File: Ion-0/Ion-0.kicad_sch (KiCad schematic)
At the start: 11 parts, among them J3 Conn_02x06_Odd_Even, J4 Conn_02x06_Odd_Even, J5 Conn_02x06_Odd_Even

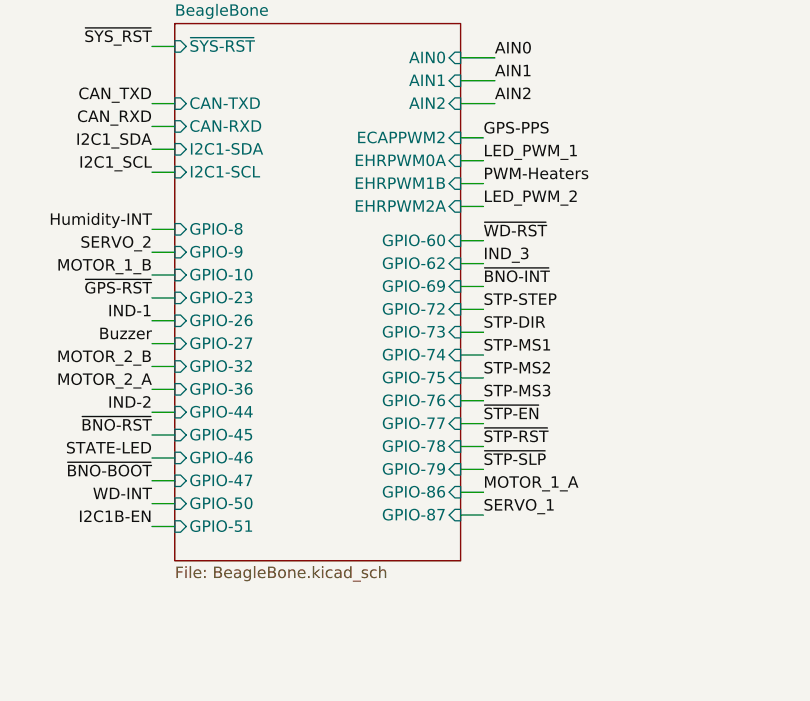
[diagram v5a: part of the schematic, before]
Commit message: version 0.8 - stepper driver included and better detailled schematic
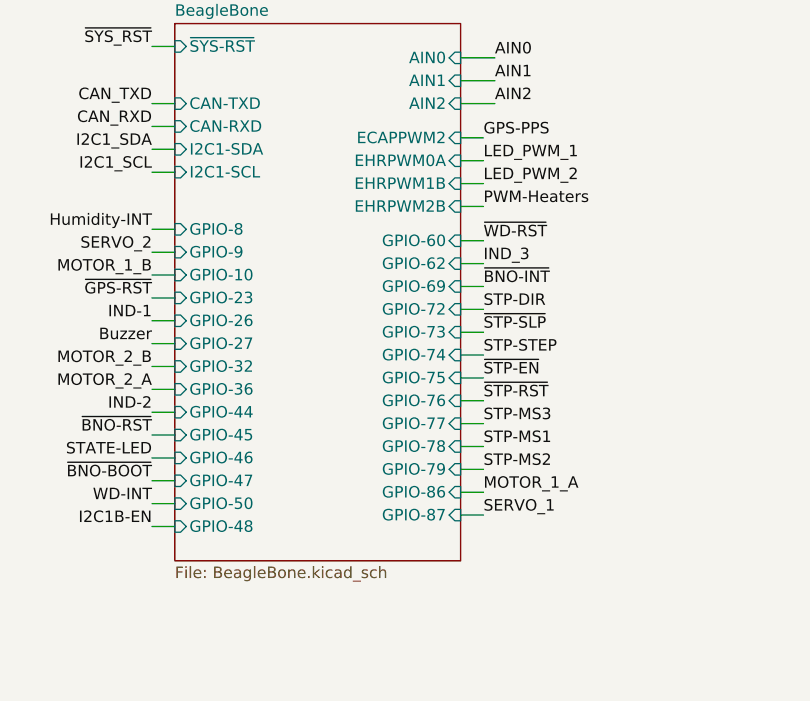
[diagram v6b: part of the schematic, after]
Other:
- sheet BeagleBone ports: added EHRPWM2B, GPIO-48; removed EHRPWM2A, GPIO-51
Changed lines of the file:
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@@
 	)
 	(label "STP-MS2"
-		(at 72.39 59.69 0)
+		(at 72.39 69.85 0)
 		(effects
 			(font
@@
 	)
 	(label "STP-DIR"
-		(at 72.39 54.61 0)
+		(at 72.39 52.07 0)
 		(effects
 			(font
@@
 	)
 	(label "STP-MS3"
-		(at 72.39 62.23 0)
+		(at 72.39 64.77 0)
 		(effects
 			(font
@@
 	)
 	(label "STP-MS1"
-		(at 72.39 57.15 0)
+		(at 72.39 67.31 0)
 		(effects
 			(font
@@
 	)
 	(label "STP-STEP"
-		(at 72.39 52.07 0)
+		(at 72.39 57.15 0)
 		(effects
 			(font
@@
 		)
 	)
-	(label ""
-		(at 231.14 81.28 0)
-		(effects
-			(font
-				(size 1.27 1.27)
-			)
-			(justify left bottom)
-		)
-	)
 	(label "CAN_RXD"
 		(at 35.56 31.75 180)
@@
 	)
 	(label "LED_PWM_2"
-		(at 72.39 40.64 0)
+		(at 72.39 38.1 0)
 		(effects
 			(font
@@
 	)
 	(label "~{STP-SLP}"
-		(at 72.39 69.85 0)
+		(at 72.39 54.61 0)
 		(effects
 			(font
@@
 	)
 	(label "PWM-Heaters"
-		(at 72.39 38.1 0)
+		(at 72.39 40.64 0)
 		(effects
 			(font
@@
 	)
 	(label "~{STP-RST}"
-		(at 72.39 67.31 0)
+		(at 72.39 62.23 0)
 		(effects
 			(font
@@
 	)
 	(label "~{STP-EN}"
-		(at 72.39 64.77 0)
+		(at 72.39 59.69 0)
 		(effects
 			(font
@@
 			)
 		)
-		(pin "EHRPWM2A" input
-			(at 69.85 40.64 0)
-			(effects
-				(font
-					(size 1.27 1.27)
-				)
-				(justify right)
-			)
-		)
 		(pin "GPIO-8" input
 			(at 38.1 43.18 180)
@@
 			)
 		)
-		(pin "GPIO-51" input
-			(at 38.1 76.2 180)
-			(effects
-				(font
-					(size 1.27 1.27)
-				)
-				(justify left)
-			)
-		)
 		(pin "GPIO-60" input
 			(at 69.85 44.45 0)
@@
 			(effects
 				(font
+					(size 1.27 1.27)
+				)
+				(justify left)
+			)
+		)
+		(pin "EHRPWM2B" input
+			(at 69.85 40.64 0)
+			(effects
+				(font
+					(size 1.27 1.27)
+				)
+				(justify right)
+			)
+		)
+		(pin "GPIO-48" input
+			(at 38.1 76.2 180)
+			(effects
+				(font
